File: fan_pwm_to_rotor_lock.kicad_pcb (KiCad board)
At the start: 2 copper layers, 69 x 40.5 mm, 12 parts, among them J1 Conn_01x04, J2 Conn_01x04, U1 LM393

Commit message: update
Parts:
- added C3: 100n, Capacitor_SMD:C_0805_2012Metric_Pad1.18x1.45mm_HandSolder, F.Cu at (56.1, 24.9)
- R1: moved to B.Cu
- U1: footprint easyeda2kicad:MINISO-8_L3.0-W3.0-P0.65-LS4.9-BL -> Package_SO:SSOP-8_2.95x2.8mm_P0.65mm
- moved J2 36.5 mm to (31.8, 22.4), turned to 90 degrees
- moved C2 19.9 mm to (64.4, 28.0)
- moved C1 19.9 mm to (64.4, 25.0)
- moved R5 14.0 mm to (47.5, 36.7)
- moved D2 13.6 mm to (58.9, 41.0), turned to 0 degrees
- moved R6 11.1 mm to (47.5, 39.7)
- moved R4 8.44 mm to (47.5, 33.8)
- moved R3 7.89 mm to (47.5, 30.8)
- moved R2 7.59 mm to (47.5, 27.9)
- moved U1 4.83 mm to (56.1, 27.6), turned to 0 degrees
- moved R1 2.59 mm to (38.6, 30.8), turned to 90 degrees
- moved J1 2.45 mm to (31.8, 33.9)
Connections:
- J1 pad 4: unconnected-(J1-Pin_4-Pad4) -> /passthrough
- J2 pad 4: unconnected-(J2-Pin_4-Pad4) -> /passthrough
- R1 pad 1: VDD -> Net-(J1-Pin_1)
- R1 pad 2: Net-(J1-Pin_1) -> VDD
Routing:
- net VDD: track 0.00 -> 2.02 mm
- net GND: track 2.97 -> 1.90 mm, vias 0 -> 2
- added copper zone on B.Cu, net GND
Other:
- board outline removed

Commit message: kaliva ton pairneis
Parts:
- added H1: MountingHole_Pad, MountingHole:MountingHole_3.2mm_M3_Pad_Via, F.Cu at (42.1, 19.3)
- R1: moved to F.Cu
- moved C1 26.7 mm to (38.7, 32.3), turned to -90 degrees
- moved C2 25.7 mm to (38.7, 28.5), turned to -90 degrees
- moved D2 20.0 mm to (39.8, 35.4), turned to 180 degrees
- moved U1 19.3 mm to (37.2, 23.6), turned to -90 degrees
- moved C3 15.3 mm to (40.8, 25.1), turned to 0 degrees
- moved R5 13.6 mm to (36.6, 28.5), turned to 90 degrees
- moved R6 13.0 mm to (40.8, 28.5), turned to -90 degrees
- moved R2 11.7 mm to (36.6, 32.3), turned to 90 degrees
- moved R3 10.2 mm to (39.5, 37.3)
- moved R4 6.85 mm to (40.8, 32.3), turned to -90 degrees
- moved R1 5.78 mm to (36.6, 36.2)
- moved J1 2.80 mm to (31.5, 36.7)
- moved J2 2.80 mm to (31.5, 25.1)
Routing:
- net Net-(U1A-+): track 0.00 -> 27.9 mm, vias 0 -> 4
- net VDD: track 2.02 -> 28.3 mm
- net /passthrough: track 0.00 -> 15.2 mm
- net Net-(U1A--): track 0.00 -> 15.1 mm, vias 0 -> 2
- net Net-(C2-Pad1): track 0.00 -> 14.4 mm
- net Net-(J1-Pin_1): track 0.00 -> 9.59 mm
- net Net-(J2-Pin_3): track 0.00 -> 8.32 mm
- net GND: track 1.90 -> 7.17 mm, vias 2 -> 4
- added copper zone on F.Cu, net VDD
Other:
- board outline added: 17.3 x 22.9 mm

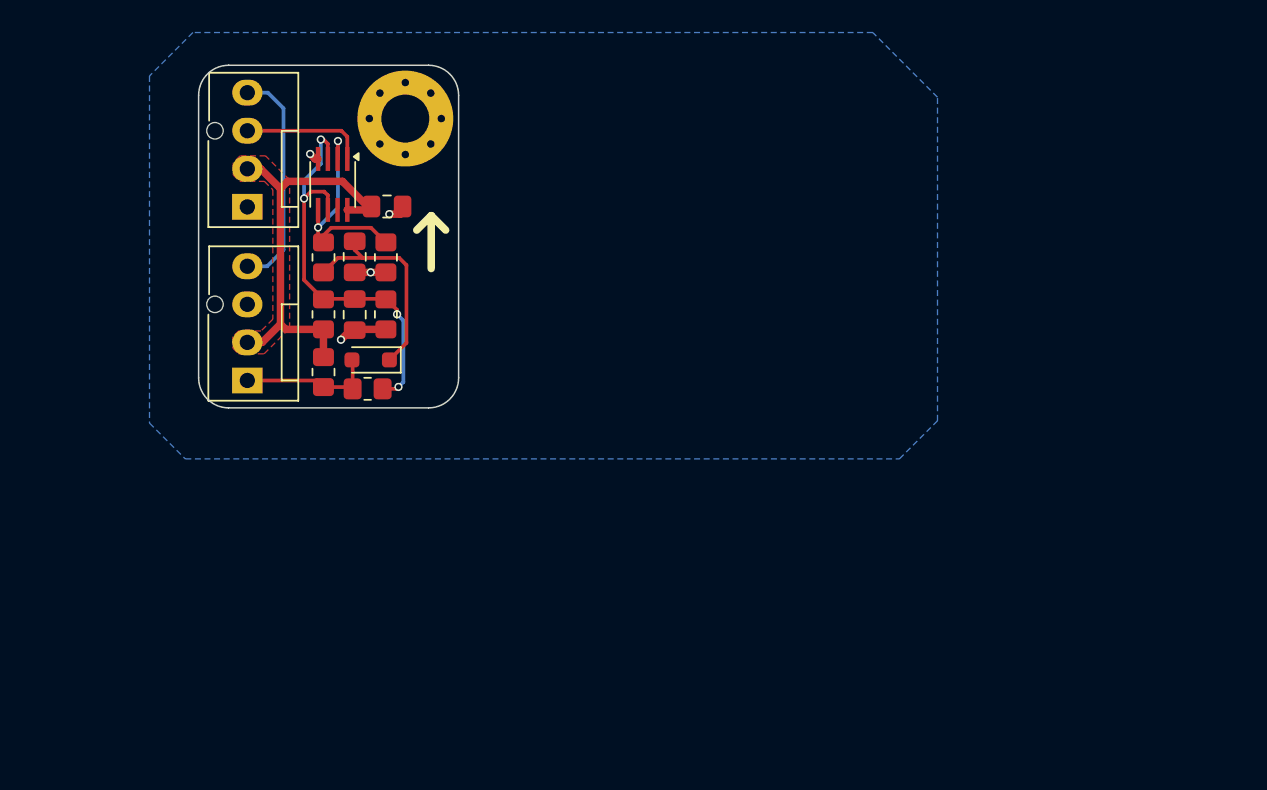
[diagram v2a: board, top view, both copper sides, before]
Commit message: Fix incorrect pin assignment
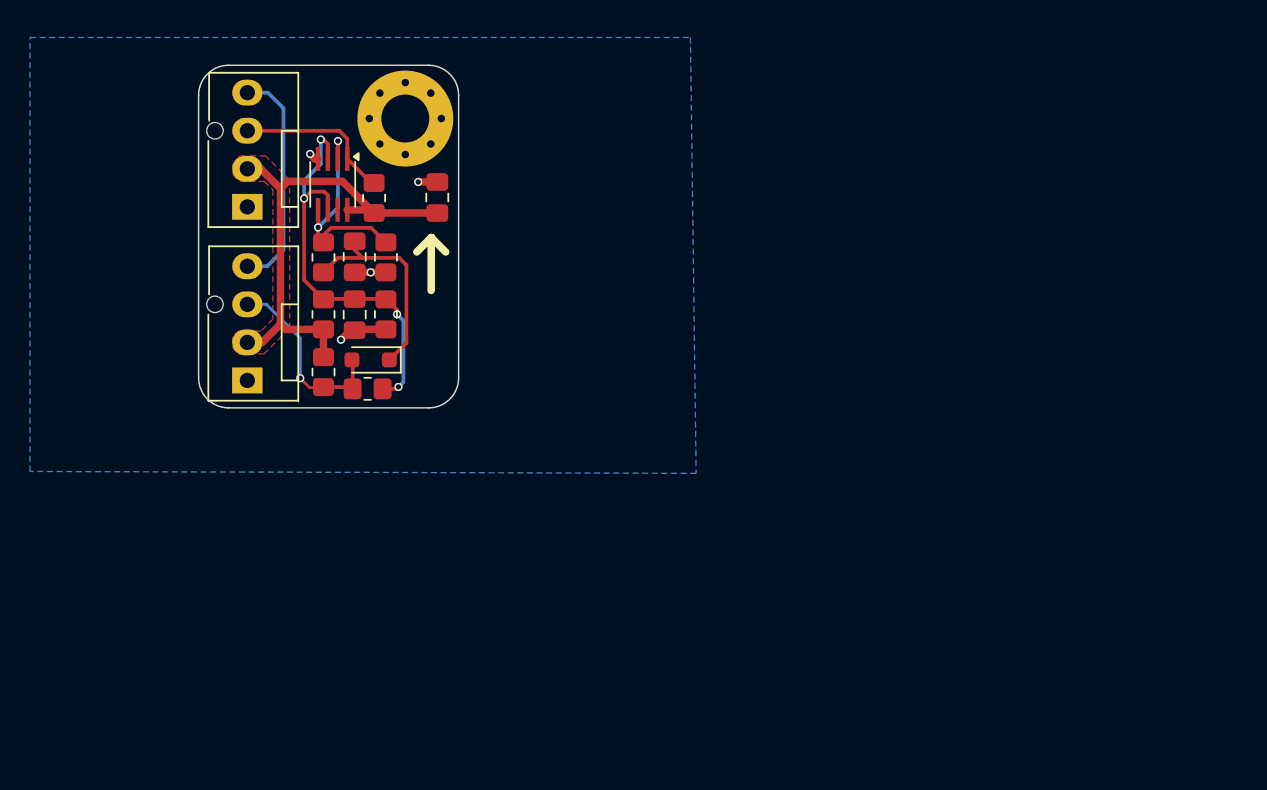
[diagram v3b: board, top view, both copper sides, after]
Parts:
- added R7: 10K, Resistor_SMD:R_0805_2012Metric_Pad1.20x1.40mm_HandSolder, F.Cu at (40.0, 24.6)
- moved C3 3.41 mm to (44.2, 24.5), turned to 90 degrees
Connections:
- D2 pad 2: Net-(J1-Pin_1) -> Net-(J1-Pin_3)
- J1 pad 1: Net-(J1-Pin_1) -> GND
- J1 pad 3: GND -> Net-(J1-Pin_3)
- R1 pad 1: Net-(J1-Pin_1) -> Net-(J1-Pin_3)
- R3 pad 1: Net-(J1-Pin_1) -> Net-(J1-Pin_3)
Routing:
- net Net-(J1-Pin_3): track 0.00 -> 13.9 mm, vias 0 -> 1
- net Net-(J1-Pin_1): track 9.59 -> 0.00 mm
- net VDD: track 28.3 -> 32.5 mm
- net Net-(J2-Pin_3): track 8.32 -> 10.7 mm
